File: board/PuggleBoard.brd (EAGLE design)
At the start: 54.6 x 86.4 mm, 136 parts, among them U1 OPA365, U10 AD5686, U11 LM2663, U12 MAX1735, U13 TLV70245, U14 REF5040, U15 AD8032, U16 24C, U2 OPA365, U3 OPA365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

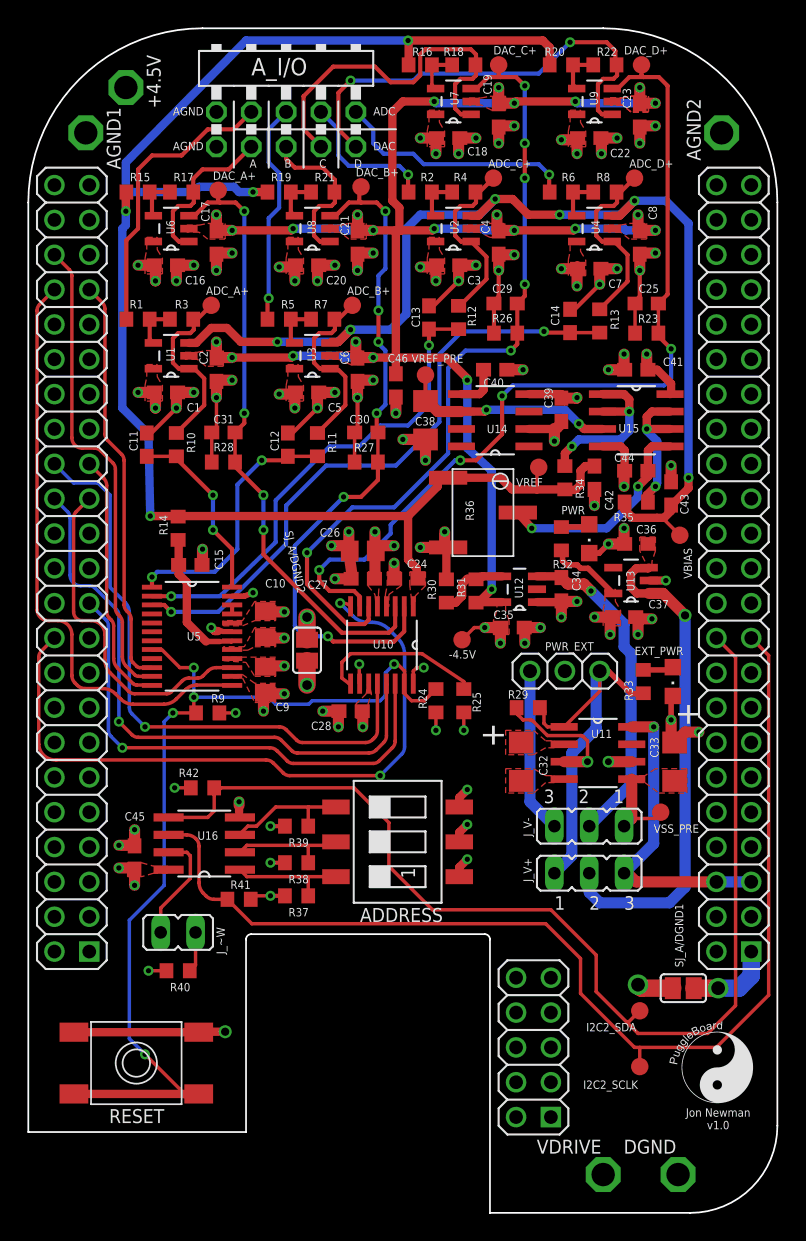
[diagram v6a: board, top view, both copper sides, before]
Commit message: Ready to print v0.1
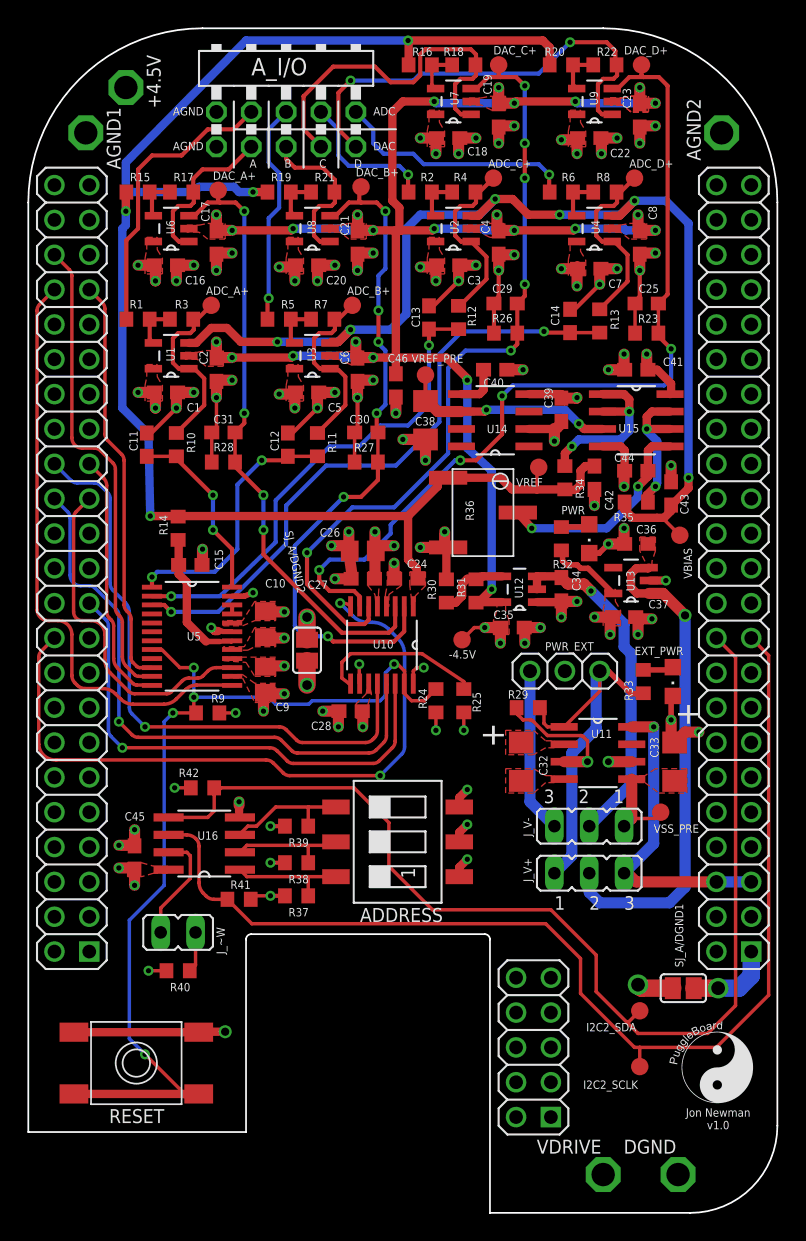
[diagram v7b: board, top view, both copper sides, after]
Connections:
- net N$23: now also U12.2
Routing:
- net AGND: track 135.9 -> 137.7 mm
- net N$23: track 24.0 -> 24.9 mm

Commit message: Started implementing changes from first build.
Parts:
- C34, C35, C36, C37: device rcl:C0603 -> rcl:C0805
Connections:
- removed net ADC_SPI4: BB1.27, U5.15
- removed net DAC_SPI3: BB1.20, U10.8
- removed net N$12: R34.2, U15.1, U15.2
- new net SPI_CLK: BB1.30, U10.12, U5.10
- new net VREF_NOFILT: R34.2, R36.1, U15.1, U15.2
- net ADC_SPI0: now also U5.11; no longer U5.10
- net ADC_SPI1: now also BB1.29, U5.12; no longer BB1.42, U5.11
- net ADC_SPI2: now also BB1.27, U5.13; no longer BB1.29, U5.12
- net ADC_SPI3: now also U5.15; no longer U5.13
- net DAC_SPI0: now also BB1.20, U10.13; no longer BB1.30, U10.12
- net DAC_SPI1: now also U10.14; no longer U10.13
- net DAC_SPI2: now also U10.8; no longer U10.14
- net VREF: no longer R36.1
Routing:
- net SPI_CLK: track 0.00 -> 72.3 mm, vias 0 -> 1
- net DAC_SPI3: track 50.6 -> 0.00 mm, vias 2 -> 0
- net DAC_SPI2: track 36.7 -> 81.7 mm, vias 1 -> 3
- net DAC_SPI0: track 43.9 -> 0.07 mm, vias 1 -> 0
- net ADC_SPI4: track 24.6 -> 0.00 mm
- net ADC_SPI3: track 43.5 -> 66.8 mm
- net ADC_SPI2: track 18.6 -> 0.00 mm
- net ADC_SPI1: track 34.7 -> 17.1 mm
- net VREF_NOFILT: track 0.00 -> 14.1 mm, vias 0 -> 2
- net N$12: track 14.1 -> 0.00 mm, vias 2 -> 0
- net VREF: track 118.8 -> 114.2 mm
- net DAC_SPI1: track 43.4 -> 39.5 mm
- net ADC_SPI0: track 29.8 -> 33.2 mm
